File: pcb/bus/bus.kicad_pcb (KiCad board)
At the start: 4 copper layers, 117.4 x 100 mm, 37 parts, among them J201 Conn_02x10_Row_Letter_First, J301 Conn_02x10_Row_Letter_First, J401 Conn_02x10_Row_Letter_First, J501 Conn_02x10_Row_Letter_First, J601 Conn_02x10_Row_Letter_First, J701 Conn_02x10_Row_Letter_First, U101 USBLC6-2SC6, U102 FE1.1s, U103 USBLC6-2SC6, U104 USBLC6-2SC6, U105 USBLC6-2SC6, U106 USBLC6-2SC6, Y101 12MHz

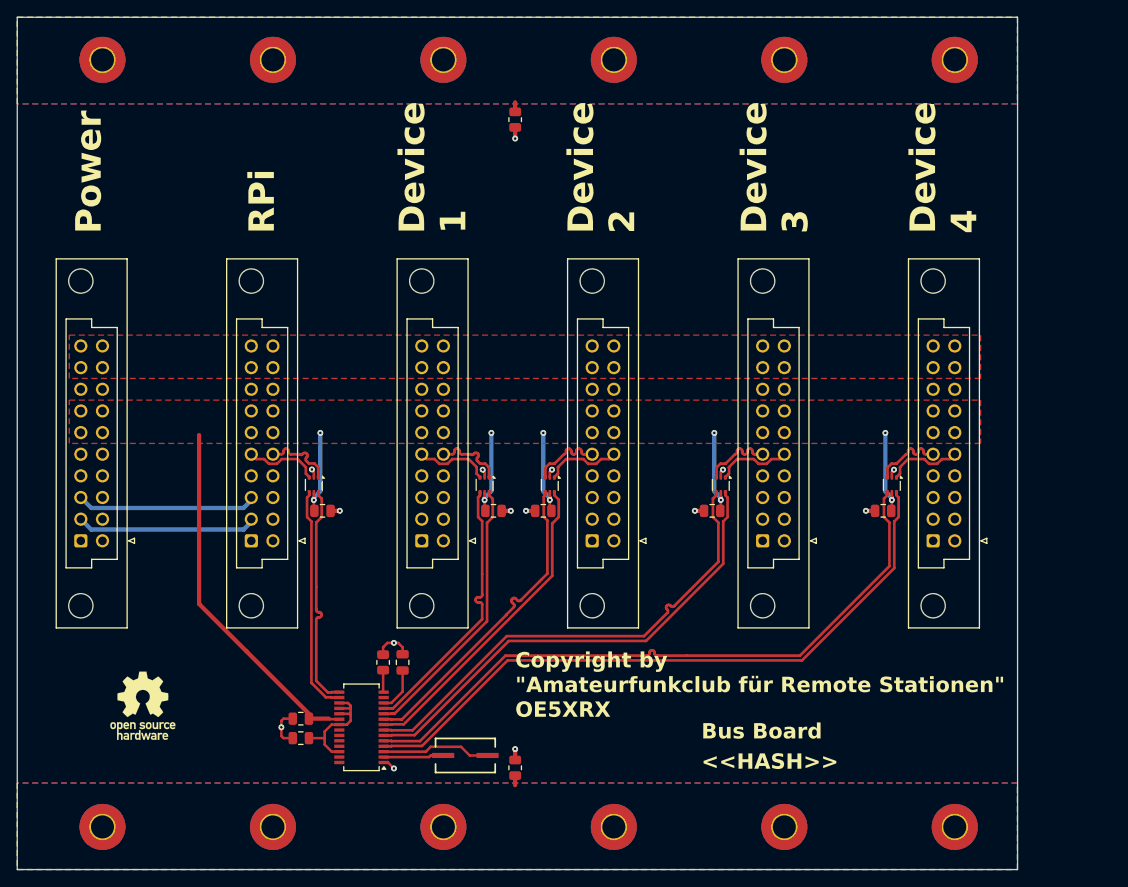
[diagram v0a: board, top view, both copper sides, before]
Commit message: update hole size
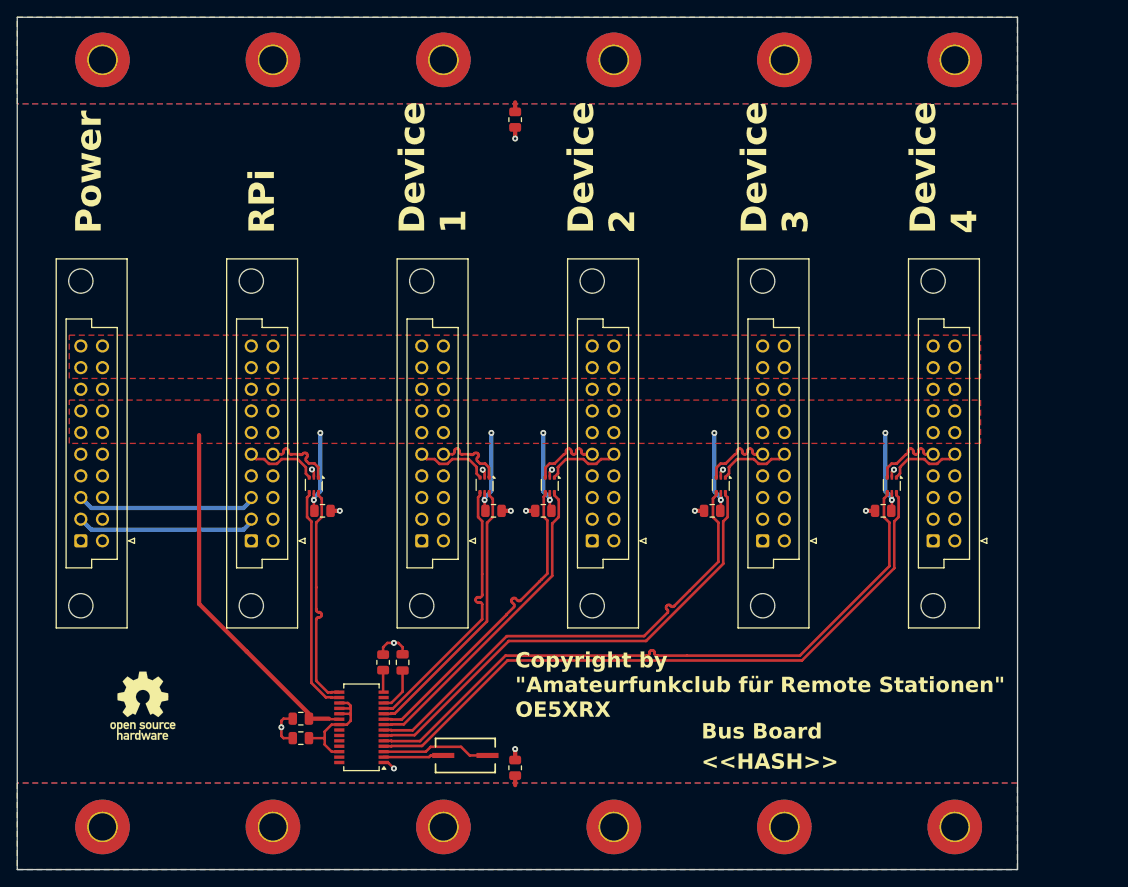
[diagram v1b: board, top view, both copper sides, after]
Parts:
- H101, H102, H103, H104, H105, H106, H109, H110, H111, H112, H113, H114: footprint MountingHole:MountingHole_2.7mm_M2.5_Pad_TopBottom -> MountingHole:MountingHole_3.2mm_M3_Pad_TopBottom

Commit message: fixes
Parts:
- removed H113, H114: MountingHole_Pad, MountingHole:MountingHole_3.2mm_M3_Pad_TopBottom
- removed R101, R102: R/C/0Ohm, Resistor_SMD:R_0805_2012Metric
- added H107: MountingHole, MountingHole:MountingHole_3.2mm_M3, F.Cu at (155.3, 120.4)
- added H108: MountingHole, MountingHole:MountingHole_3.2mm_M3, F.Cu at (175.3, 120.4)
- H101, H102, H103, H104, H105, H106, H109, H110, H111, H112: value MountingHole_Pad -> MountingHole; footprint MountingHole:MountingHole_3.2mm_M3_Pad_TopBottom -> MountingHole:MountingHole_3.2mm_M3
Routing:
- net GND: track 23.4 -> 20.8 mm, vias 15 -> 13
- net /GND_TOP_MH: track 1.12 -> 0.00 mm
- net /GND_BOTTOM_MH: track 1.12 -> 0.00 mm
- removed copper zone on B.Cu, net /GND_BOTTOM_MH
- removed copper zone on F.Cu, net /GND_BOTTOM_MH
- removed copper zone on B.Cu, net /GND_TOP_MH
- removed copper zone on F.Cu, net /GND_TOP_MH

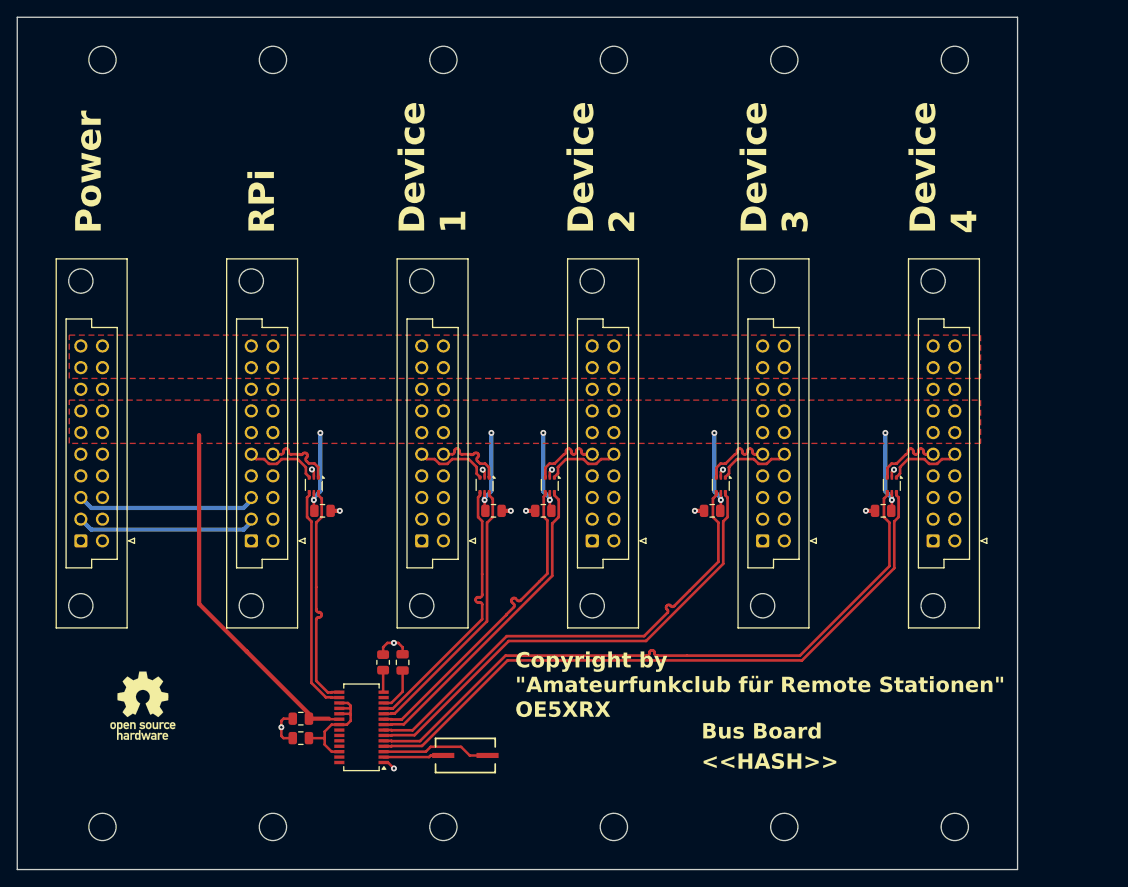
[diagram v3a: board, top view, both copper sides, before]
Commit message: create more space for 3d printed parts
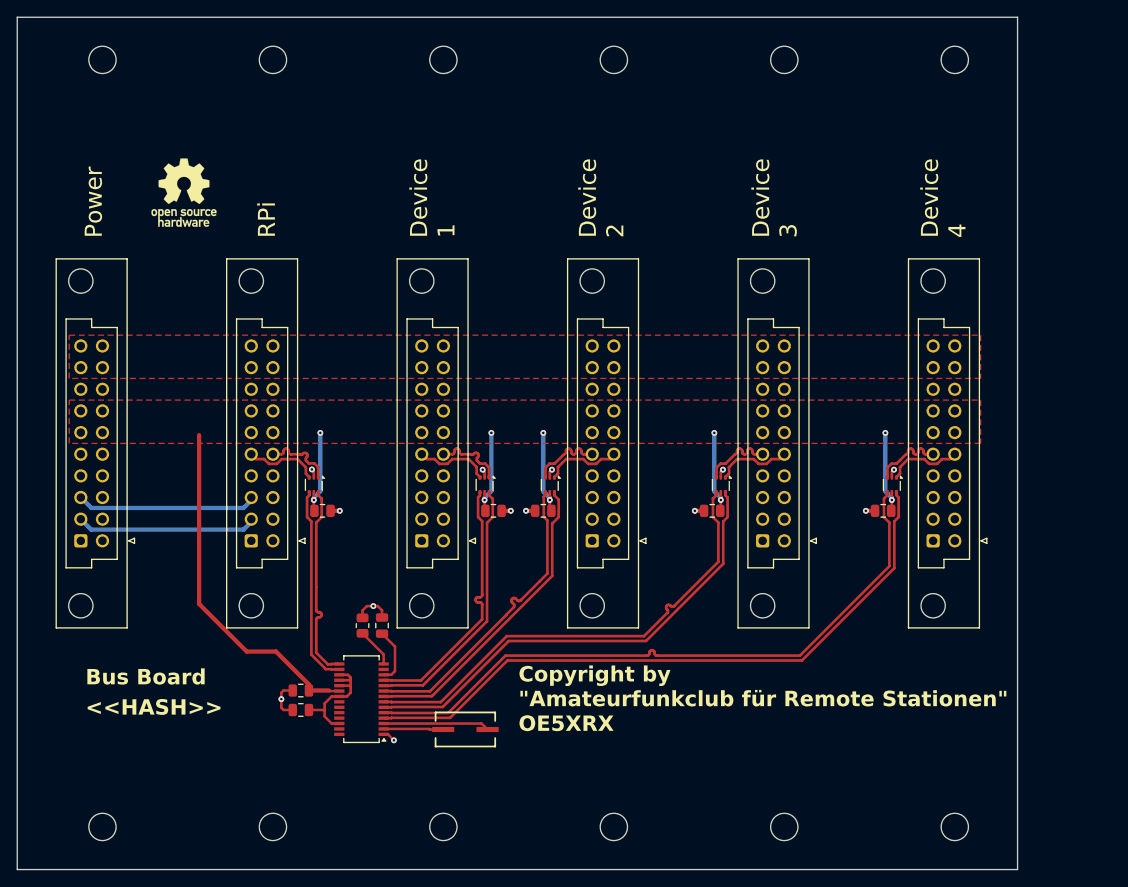
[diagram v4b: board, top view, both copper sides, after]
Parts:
- moved #SYM101 60.4 mm to (84.8, 46.0)
- moved C102 4.95 mm to (108.1, 96.8)
- moved R103 4.95 mm to (105.8, 96.8)
- moved C101 3.30 mm to (98.6, 106.7)
- moved C103 3.30 mm to (98.6, 104.4)
- moved U102 3.30 mm to (105.7, 105.4)
- moved Y101 3.05 mm to (117.9, 109.0)
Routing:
- net /MASTER_USB+: track 26.7 -> 23.4 mm
- net /MASTER_USB-: track 26.6 -> 23.3 mm
- net Net-(U102-REXT): track 2.69 -> 4.71 mm
- net /USB2+: track 37.3 -> 36.0 mm
- net /USB3+: track 56.9 -> 55.5 mm
- net /USB2-: track 37.4 -> 36.0 mm
- net /USB1-: track 32.2 -> 30.9 mm
- net /USB4-: track 77.8 -> 76.4 mm
- net /USB4+: track 77.8 -> 76.4 mm
- net /USB3-: track 56.9 -> 55.6 mm
- net /USB1+: track 32.4 -> 31.0 mm
- net /VD18: track 5.26 -> 6.54 mm
- net +5V: track 90.6 -> 89.9 mm
